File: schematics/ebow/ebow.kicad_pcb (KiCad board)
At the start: 2 copper layers, 70 x 30 mm, 17 parts, among them SW1 SW_SPDT, U1 LM386

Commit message: more edits
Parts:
- moved H2 45.6 mm to (164.1, 116.1)
- moved H1 45.4 mm to (197.6, 116.3)
- moved R4 23.1 mm to (194.7, 113.3), turned to 0 degrees
- turned L1 to 0 degrees
- turned L2 to 180 degrees
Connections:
- L1 pad 1: GND -> Net-(U1-+)
- L1 pad 2: Net-(U1-+) -> GND
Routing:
- net GND: track 0.00 -> 109.0 mm
- net Net-(SW1-B): track 0.00 -> 79.4 mm
- net Net-(D1-A): track 0.00 -> 20.9 mm
- net Net-(U1-+): track 0.00 -> 20.3 mm
- net Net-(C5-Pad1): track 0.00 -> 19.8 mm
- net Net-(U1-BYPASS): track 0.00 -> 8.68 mm
- net Net-(C5-Pad2): track 0.00 -> 7.79 mm
- net Net-(C1-Pad1): track 0.00 -> 6.41 mm
- net Net-(C1-Pad2): track 0.00 -> 5.81 mm
- net +9V: track 0.00 -> 5.49 mm
- added copper zone on F.Cu, net GND
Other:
- board text added: "Input Coil"
- board text added: "Output Coil"

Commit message: completed first pcb
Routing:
- net GND: track 109.0 -> 108.4 mm
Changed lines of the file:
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@@
-	)
-	(segment
-		(start 168.357 109.982)
-		(end 154.94 109.982)
-		(width 0.6)
-		(layer "F.Cu")
-		(net 4)
 	)
 	(segment
@@
 	)
 	(segment
-		(start 154.94 109.22)
-		(end 154.914 109.194)
+		(start 174.077 115.702)
+		(end 170.2845 111.9095)
 		(width 0.6)
 		(layer "F.Cu")
@@
 	)
 	(segment
-		(start 154.94 109.982)
-		(end 154.94 109.22)
+		(start 154.914 104.902)
+		(end 154.914 108.94)
+		(width 0.6)
+		(layer "F.Cu")
+		(net 4)
+	)
+	(segment
+		(start 154.914 108.94)
+		(end 157.736 111.762)
 		(width 0.6)
 		(layer "F.Cu")
@@
 		(end 177.356 106.3122)
 		(width 0.3)
+		(layer "F.Cu")
+		(net 4)
+	)
+	(segment
+		(start 170.137 111.762)
+		(end 170.2845 111.9095)
+		(width 0.6)
 		(layer "F.Cu")
 		(net 4)
@@
 	)
 	(segment
-		(start 174.077 115.702)
-		(end 168.357 109.982)
+		(start 157.736 111.762)
+		(end 170.137 111.762)
 		(width 0.6)
 		(layer "F.Cu")
-		(net 4)
-	)
-	(segment
-		(start 154.914 109.194)
-		(end 154.914 104.902)
-		(width 0.6)
-		(layer "F.Cu")

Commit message: corrections
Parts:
- added FID3: Fiducial, Fiducial:Fiducial_0.5mm_Mask1.5mm, F.Cu at (164.0, 116.0)
- R1, R4: footprint Resistor_SMD:R_0201_0603Metric -> Resistor_SMD:R_0201_0603Metric_Pad0.64x0.40mm_HandSolder
- moved H2 22.6 mm to (165.5, 93.5)
- moved FID2 1.89 mm to (170.0, 116.0)
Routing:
- net GND: track 108.4 -> 13.4 mm
- net Net-(SW1-B): track 79.4 -> 55.6 mm

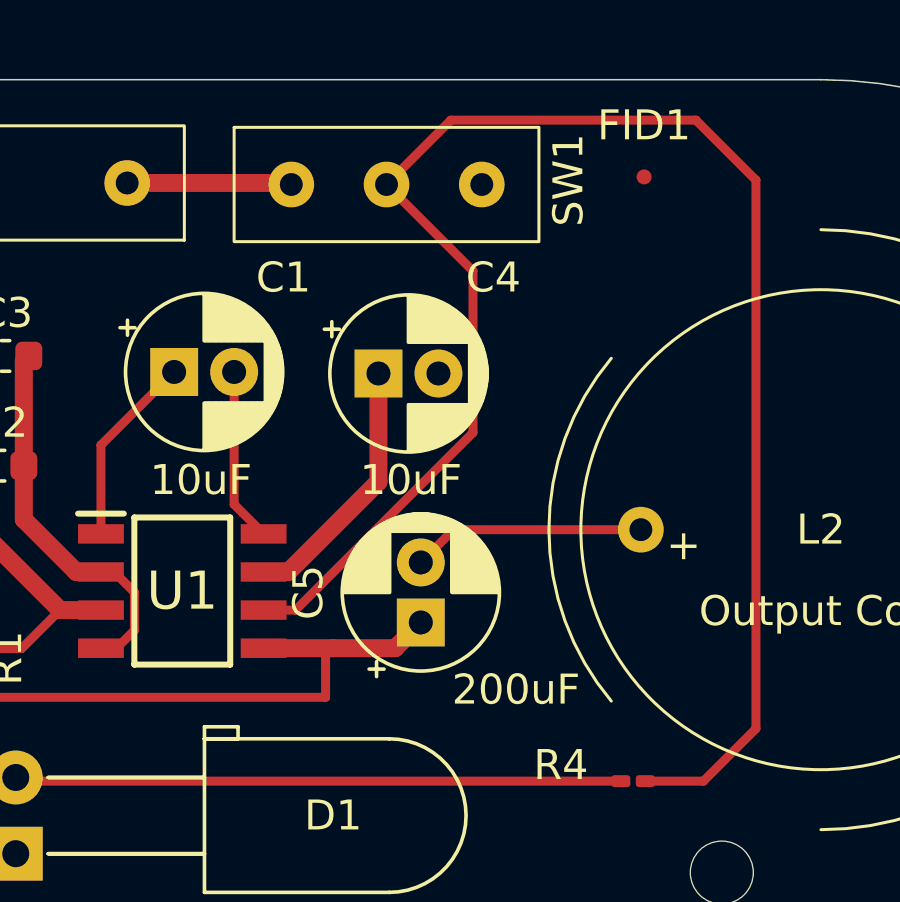
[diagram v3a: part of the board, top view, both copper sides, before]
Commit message: updated to fix DRC errors
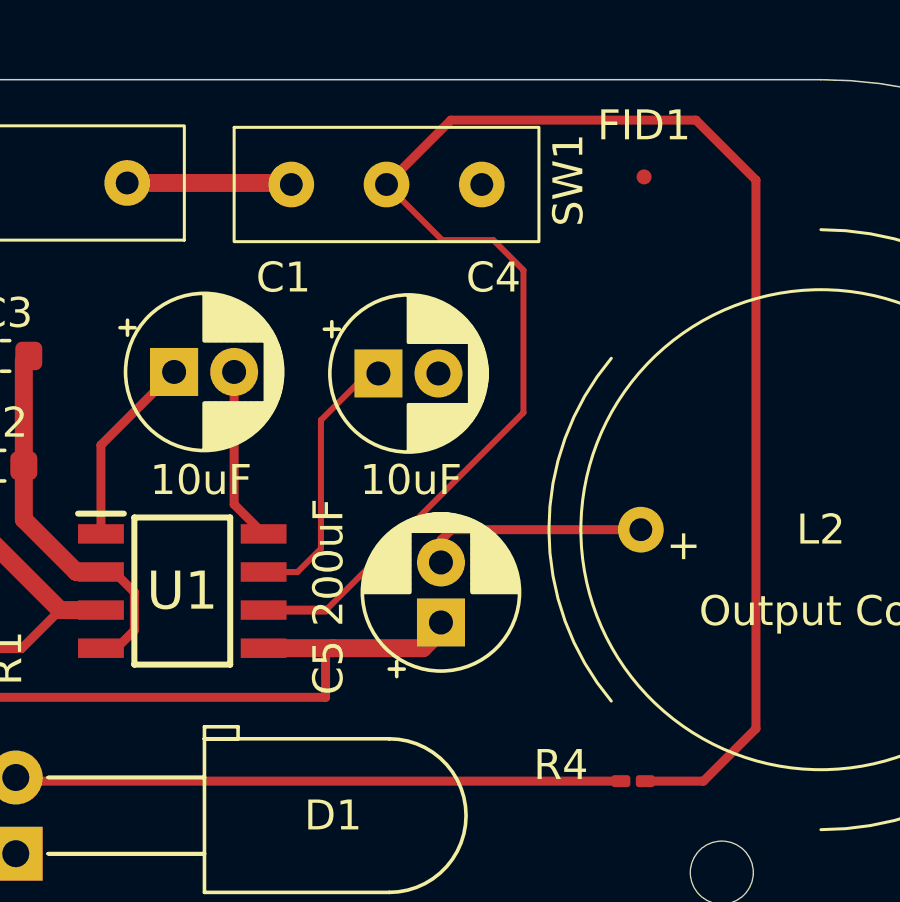
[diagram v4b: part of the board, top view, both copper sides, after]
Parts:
- moved C5 0.67 mm to (188.2, 108.0)
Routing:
- net Net-(SW1-B): track 55.6 -> 58.6 mm
- net Net-(C5-Pad1): track 19.8 -> 20.7 mm
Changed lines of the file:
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@@
 			(layer "F.Fab")
 		)
-		(fp_text user "${REFERENCE}"
-			(at 1 0 0)
-			(layer "F.Fab")
-			(effects
-				(font
-					(size 1 1)
-					(thickness 0.15)
-				)
-			)
-		)
 		(pad "1" thru_hole rect
 			(at 0 0)
@@
 	(footprint "Capacitor_THT:CP_Radial_D5.0mm_P2.00mm"
 		(layer "F.Cu")
-		(at 187.579 107.9942 90)
+		(at 188.25 107.9942 90)
 		(descr "CP, Radial series, Radial, pin pitch=2.00mm, , diameter=5mm, Electrolytic Capacitor")
 		(tags "CP Radial series Radial pin pitch 2.00mm  diameter 5mm Electrolytic Capacitor")
 		(property "Reference" "C5"
-			(at 1 -3.75 90)
+			(at -1.5058 -3.75 90)
 			(layer "F.SilkS")
 			(effects
@@
 		)
 		(property "Value" "200uF"
-			(at -2.2418 3.175 0)
+			(at 1.9942 -3.75 90)
 			(layer "F.SilkS")
 			(effects
@@
 	)
 	(segment
-		(start 186.166688 103.303512)
+		(start 185.805 99.695)
 		(end 186.166688 99.695)
-		(width 0.6)
+		(width 0.2)
 		(layer "F.Cu")
 		(net 5)
 	)
 	(segment
-		(start 183.158 106.3122)
-		(end 186.166688 103.303512)
-		(width 0.6)
+		(start 184.25 101.25)
+		(end 185.805 99.695)
+		(width 0.2)
+		(layer "F.Cu")
+		(net 5)
+	)
+	(segment
+		(start 183.469504 106.3122)
+		(end 184.25 105.531704)
+		(width 0.2)
 		(layer "F.Cu")
 		(net 5)
@@
 	(segment
 		(start 182.339 106.3122)
-		(end 183.158 106.3122)
-		(width 0.6)
+		(end 183.469504 106.3122)
+		(width 0.2)
 		(layer "F.Cu")
 		(net 5)
 	)
 	(segment
-		(start 194.914 104.902)
-		(end 188.6712 104.902)
+		(start 184.25 105.531704)
+		(end 184.25 101.25)
+		(width 0.2)
+		(layer "F.Cu")
+		(net 5)
+	)
+	(segment
+		(start 188.25 105.25)
+		(end 188.598 104.902)
+		(width 0.3)
+		(layer "F.Cu")
+		(net 6)
+	)
+	(segment
+		(start 188.598 104.902)
+		(end 194.914 104.902)
 		(width 0.3)
 		(layer "F.Cu")
@@
 	)
 	(segment
-		(start 188.6712 104.902)
-		(end 187.579 105.9942)
+		(start 188.25 105.9942)
+		(end 188.25 105.25)
 		(width 0.3)
 		(layer "F.Cu")
@@
 	)
 	(segment
-		(start 172.7454 109.504)
-		(end 172.7454 110.2614)
-		(width 0.3)
+		(start 187.6478 108.8522)
+		(end 184.658 108.8522)
+		(width 0.6)
 		(layer "F.Cu")
 		(net 7)
 	)
 	(segment
-		(start 184.658 108.8522)
-		(end 182.339 108.8522)
+		(start 188.25 107.9942)
+		(end 188.25 108.25)
 		(width 0.6)
 		(layer "F.Cu")
@@
 	)
 	(segment
-		(start 186.721 108.8522)
-		(end 184.658 108.8522)
+		(start 188.25 108.25)
+		(end 187.6478 108.8522)
 		(width 0.6)
 		(layer "F.Cu")
@@
 	)
 	(segment
-		(start 184.404 109.1062)
-		(end 184.658 108.8522)
+		(start 172.7454 109.504)
+		(end 172.7454 110.2614)
 		(width 0.3)
 		(layer "F.Cu")
@@
 	)
 	(segment
-		(start 172.7454 110.2614)
-		(end 172.974 110.49)
+		(start 184.658 108.8522)
+		(end 182.339 108.8522)
+		(width 0.6)
+		(layer "F.Cu")
+		(net 7)
+	)
+	(segment
+		(start 184.404 109.1062)
+		(end 184.658 108.8522)
 		(width 0.3)
 		(layer "F.Cu")
@@
 	)
 	(segment
-		(start 187.579 107.9942)
-		(end 186.721 108.8522)
-		(width 0.6)
+		(start 172.7454 110.2614)
+		(end 172.974 110.49)
+		(width 0.3)
 		(layer "F.Cu")
 		(net 7)
@@
 	)
 	(segment
-		(start 189.317688 96.277488)
-		(end 189.317688 101.667512)
+		(start 198.75 93.25)
+		(end 198.75 111.534)
 		(width 0.3)
 		(layer "F.Cu")
@@
 	)
 	(segment
-		(start 189.317688 101.667512)
-		(end 183.403 107.5822)
-		(width 0.3)
+		(start 190 95.25)
+		(end 188.2902 95.25)
+		(width 0.2)
 		(layer "F.Cu")
 		(net 10)
 	)
 	(segment
-		(start 198.75 93.25)
-		(end 198.75 111.534)
+		(start 196.75 91.25)
+		(end 198.75 93.25)
 		(width 0.3)
 		(layer "F.Cu")
@@
 	)
 	(segment
-		(start 186.436 93.3958)
-		(end 189.317688 96.277488)
-		(width 0.3)
+		(start 188.2902 95.25)
+		(end 186.436 93.3958)
+		(width 0.2)
 		(layer "F.Cu")
 		(net 10)
 	)
 	(segment
-		(start 196.75 91.25)
-		(end 198.75 93.25)
-		(width 0.3)
+		(start 191 96.25)
+		(end 190 95.25)
+		(width 0.2)
+		(layer "F.Cu")
+		(net 10)
+	)
+	(segment
+		(start 184.4178 107.5822)
+		(end 191 101)
+		(width 0.2)
 		(layer "F.Cu")
 		(net 10)
@@
 	)
 	(segment
+		(start 191 101)
+		(end 191 96.25)
+		(width 0.2)
+		(layer "F.Cu")
+		(net 10)
+	)
+	(segment
 		(start 188.5818 91.25)
 		(end 196.75 91.25)
@@
 	)
 	(segment
-		(start 183.403 107.5822)
-		(end 182.339 107.5822)
+		(start 197 113.284)
+		(end 195.0625 113.284)
 		(width 0.3)
 		(layer "F.Cu")
@@
 	)
 	(segment
-		(start 197 113.284)
-		(end 195.0625 113.284)
+		(start 182.339 107.5822)
+		(end 184.4178 107.5822)
 		(width 0.3)
 		(layer "F.Cu")
@@
 		(priority 1)
 		(connect_pads
-			(clearance 0.3)
+			(clearance 0.2)
 		)
 		(min_thickness 0.25)

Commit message: fixed ground
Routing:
- net GND: track 13.4 -> 16.7 mm, vias 0 -> 4
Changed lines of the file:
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@@
 			(layer "F.Fab")
-		)
-		(fp_text user "${REFERENCE}"
-			(at 0 -0.68 270)
-			(layer "F.Fab")
-			(effects
-				(font
-					(size 0.25 0.25)
-					(thickness 0.04)
-				)
-			)
 		)
 		(pad "" smd roundrect
@@
 		)
 	)
+	(dimension
+		(type orthogonal)
+		(layer "Dwgs.User")
+		(pts
+			(xy 145.914 104.902) (xy 215.914 104.902)
+		)
+		(height -28.402)
+		(orientation 0)
+		(format
+			(prefix "")
+			(suffix "")
+			(units 3)
+			(units_format 1)
+			(precision 4)
+		)
+		(style
+			(thickness 0.2)
+			(arrow_length 1.27)
+			(text_position_mode 0)
+			(arrow_direction outward)
+			(extension_height 0.58642)
+			(extension_offset 0.5)
+			(keep_text_aligned yes)
+		)
+		(gr_text "70.0000 mm"
+			(at 180.914 74.7 0)
+			(layer "Dwgs.User")
+			(effects
+				(font
+					(size 1.5 1.5)
+					(thickness 0.3)
+				)
+			)
+		)
+	)
+	(dimension
+		(type orthogonal)
+		(layer "Dwgs.User")
+		(pts
+			(xy 200.914 89.902) (xy 200.914 119.902)
+		)
+		(height 34.836)
+		(orientation 1)
+		(format
+			(prefix "")
+			(suffix "")
+			(units 3)
+			(units_format 1)
+			(precision 4)
+		)
+		(style
+			(thickness 0.2)
+			(arrow_length 1.27)
+			(text_position_mode 0)
+			(arrow_direction outward)
+			(extension_height 0.58642)
+			(extension_offset 0.5)
+			(keep_text_aligned yes)
+		)
+		(gr_text "30.0000 mm"
+			(at 233.95 104.902 90)
+			(layer "Dwgs.User")
+			(effects
+				(font
+					(size 1.5 1.5)
+					(thickness 0.3)
+				)
+			)
+		)
+	)
 	(segment
 		(start 176.917 105.0422)
@@
 	)
 	(segment
-		(start 178.031 108.2572)
-		(end 178.031 106.9872)
-		(width 0.3)
-		(layer "F.Cu")
-		(net 4)
-	)
-	(segment
-		(start 177.356 106.3122)
-		(end 176.917 106.3122)
-		(width 0.3)
-		(layer "F.Cu")
-		(net 4)
-	)
-	(segment
 		(start 176.917 108.8522)
 		(end 177.436 108.8522)
@@
 	)
 	(segment
-		(start 177.436 108.8522)
-		(end 178.031 108.2572)
+		(start 175.924318 99.1108)
+		(end 175.949114 99.086004)
+		(width 0.3)
+		(layer "F.Cu")
+		(net 4)
+	)
+	(segment
+		(start 177.0192 108.75)
+		(end 176.917 108.8522)
+		(width 0.3)
+		(layer "F.Cu")
+		(net 4)
+	)
+	(segment
+		(start 174.3456 102.7684)
+		(end 175.784104 102.7684)
+		(width 0.3)
+		(layer "F.Cu")
+		(net 4)
+	)
+	(segment
+		(start 174.511 99.1108)
+		(end 175.924318 99.1108)
 		(width 0.3)
 		(layer "F.Cu")
@@
 	)
 	(segment
+		(start 178.75 108.75)
+		(end 177.0192 108.75)
+		(width 0.3)
+		(layer "F.Cu")
+		(net 4)
+	)
+	(segment
+		(start 175.0179 105.2321)
+		(end 176.098 106.3122)
+		(width 0.6)
+		(layer "F.Cu")
+		(net 4)
+	)
+	(segment
+		(start 175.784104 102.7684)
+		(end 175.862903 102.689601)
+		(width 0.3)
+		(layer "F.Cu")
+		(net 4)
+	)
+	(segment
 		(start 174.3456 104.5598)
-		(end 176.098 106.3122)
-		(width 0.6)
-		(layer "F.Cu")
-		(net 4)
-	)
-	(segment
-		(start 178.031 106.9872)
-		(end 177.356 106.3122)
-		(width 0.3)
+		(end 175.0179 105.2321)
+		(width 0.6)
+		(layer "F.Cu")
+		(net 4)
+	)
+	(segment
+		(start 178.6878 106.3122)
+		(end 178.75 106.25)
+		(width 0.3)
+		(layer "F.Cu")
+		(net 4)
+	)
+	(segment
+		(start 176.917 106.3122)
+		(end 178.6878 106.3122)
+		(width 0.3)
+		(layer "F.Cu")
+		(net 4)
+	)
+	(segment
+		(start 174.3456 101)
+		(end 174.3456 99.2762)
+		(width 0.6)
 		(layer "F.Cu")
 		(net 4)
@@
 	(segment
 		(start 174.3456 102.7684)
-		(end 174.3456 99.2762)
-		(width 0.6)
-		(layer "F.Cu")
-		(net 4)
-	)
+		(end 174.3456 101)
+		(width 0.6)
+		(layer "F.Cu")
+		(net 4)
+	)
+	(via
+		(at 175.949114 99.086004)
+		(size 0.6)
+		(drill 0.3)
+		(layers "F.Cu" "B.Cu")
+		(net 4)
+	)
+	(via
+		(at 178.75 108.75)
+		(size 0.6)
+		(drill 0.3)
+		(layers "F.Cu" "B.Cu")
+		(free yes)
+		(net 4)
+	)
+	(via
+		(at 175.862903 102.689601)
+		(size 0.6)
+		(drill 0.3)
+		(layers "F.Cu" "B.Cu")
+		(net 4)
+	)
+	(via
+		(at 178.75 106.25)
+		(size 0.6)
+		(drill 0.3)
+		(layers "F.Cu" "B.Cu")
+		(free yes)
+		(net 4)
+	)

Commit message: added board characteristics
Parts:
- moved BT1 33.6 mm to (208.2, 99.3)
- moved C1 33.6 mm to (212.4, 105.7)
- moved C2 33.6 mm to (206.6, 108.9)
- moved C3 33.6 mm to (206.7, 105.2)
- moved C4 33.6 mm to (219.2, 105.8)
- moved C5 33.6 mm to (221.2, 114.1)
- moved D1 33.6 mm to (207.1, 121.8)
- moved FID1 33.6 mm to (228.0, 99.2)
- moved FID2 33.6 mm to (203.0, 122.1)
- moved FID3 33.6 mm to (197.0, 122.1)
- moved H1 33.6 mm to (230.6, 122.4)
- moved H2 33.6 mm to (198.5, 99.6)
- moved L1 33.6 mm to (193.9, 111.0)
- moved L2 33.6 mm to (233.9, 111.0)
- moved R1 33.6 mm to (205.7, 115.3)
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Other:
- board text added: "0"
- board text added: "0 mm"
- board text added: "0.0000 mm / 0.0000 mm"
- board text added: "0.01 mm"
- board text added: "0.02"
- board text added: "0.035 mm"
- board text added: "0.3000 mm"
- board text added: "1"
- board text added: "1.51 mm"
- board text added: "1.6000 mm"
- board text added: "2"
- board text added: "3.3"
- board text added: "4.5"
- board text added: "70.0050 mm x 30.0000 mm"
- board text added: "B.Cu"
- board text added: "B.Mask"
- board text added: "B.Paste"
- board text added: "B.Silkscreen"
- board text added: "BOARD CHARACTERISTICS"
- board text added: "Board Thickness:"
- board text added: "Board overall dimensions:"
- board text added: "Bottom Silk Screen"
- board text added: "Bottom Solder Mask"
- board text added: "Bottom Solder Paste"
- board text added: "Castellated pads:"
- board text added: "Color"
- board text added: "Copper Finish:"
- board text added: "Copper Layer Count:"
- board text added: "Dielectric"
- board text added: "Edge card connectors:"
- board text added: "Epsilon R"
- board text added: "F.Cu"
- board text added: "F.Mask"
- board text added: "F.Paste"
- board text added: "F.Silkscreen"
- board text added: "FR4"
- board text added: "Impedance Control:"
- board text added: "Layer Name"
- board text added: "Loss Tangent"
- board text added: "Material"
- board text added: "Min hole diameter:"
- board text added: "Min track/spacing:"
- board text added: "No"
- board text added: "None"
- board text added: "Not specified"
- board text added: "Plated Board Edge:"
- board text added: "Thickness (mm)"
- board text added: "Top Silk Screen"
- board text added: "Top Solder Mask"
- board text added: "Top Solder Paste"
- board text added: "Type"
- board text added: "copper"
- board text added: "core"
